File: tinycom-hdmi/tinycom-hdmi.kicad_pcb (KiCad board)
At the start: 2 copper layers, 45.2 x 45.2 mm, 70 parts, among them J1 MICRO_SD_HINGE, P1 CONN_02X10, P2 CONN_02X10, P4 USB_OTG, U1 SY8008BAAC, U2 AXP209, U3 SY8008BAAC, U4 RTL8188, U5 rainsun-antenna, U6 RCLAMP0524P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

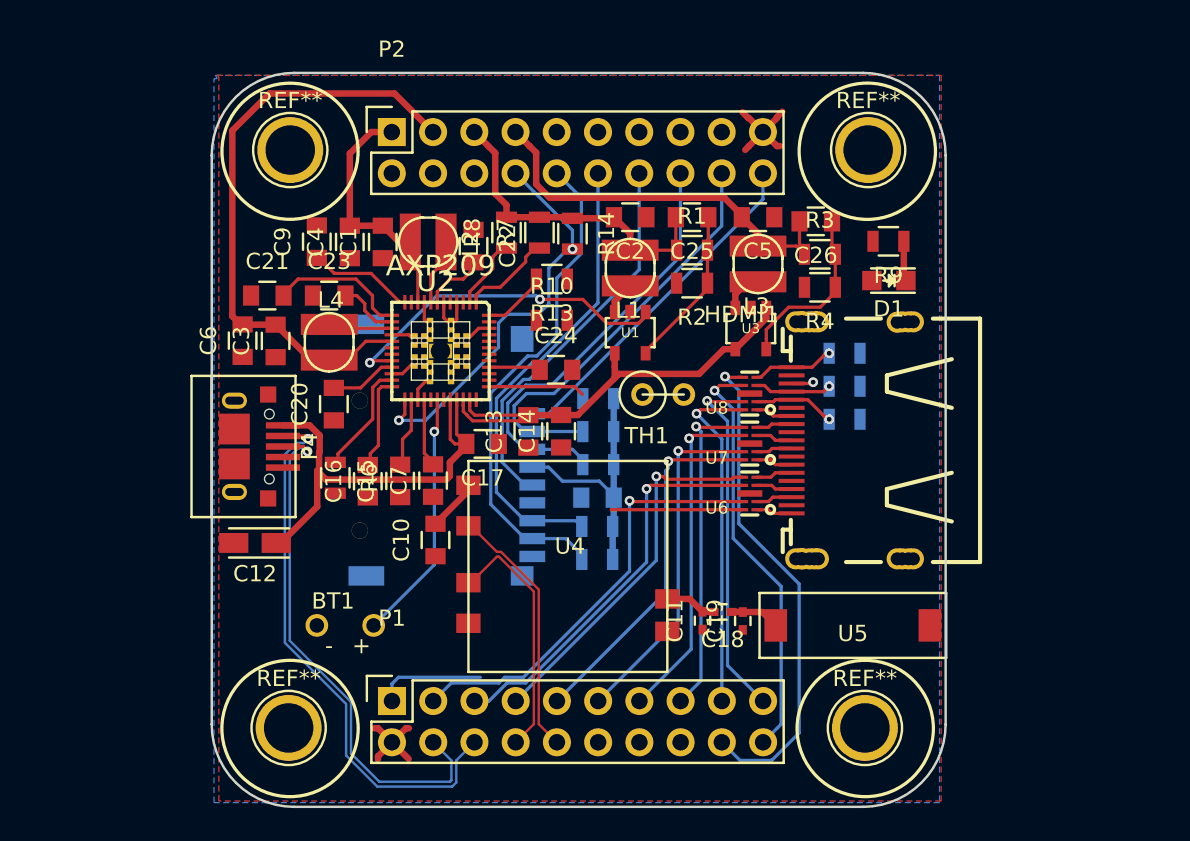
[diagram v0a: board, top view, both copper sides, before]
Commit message: hdmi route
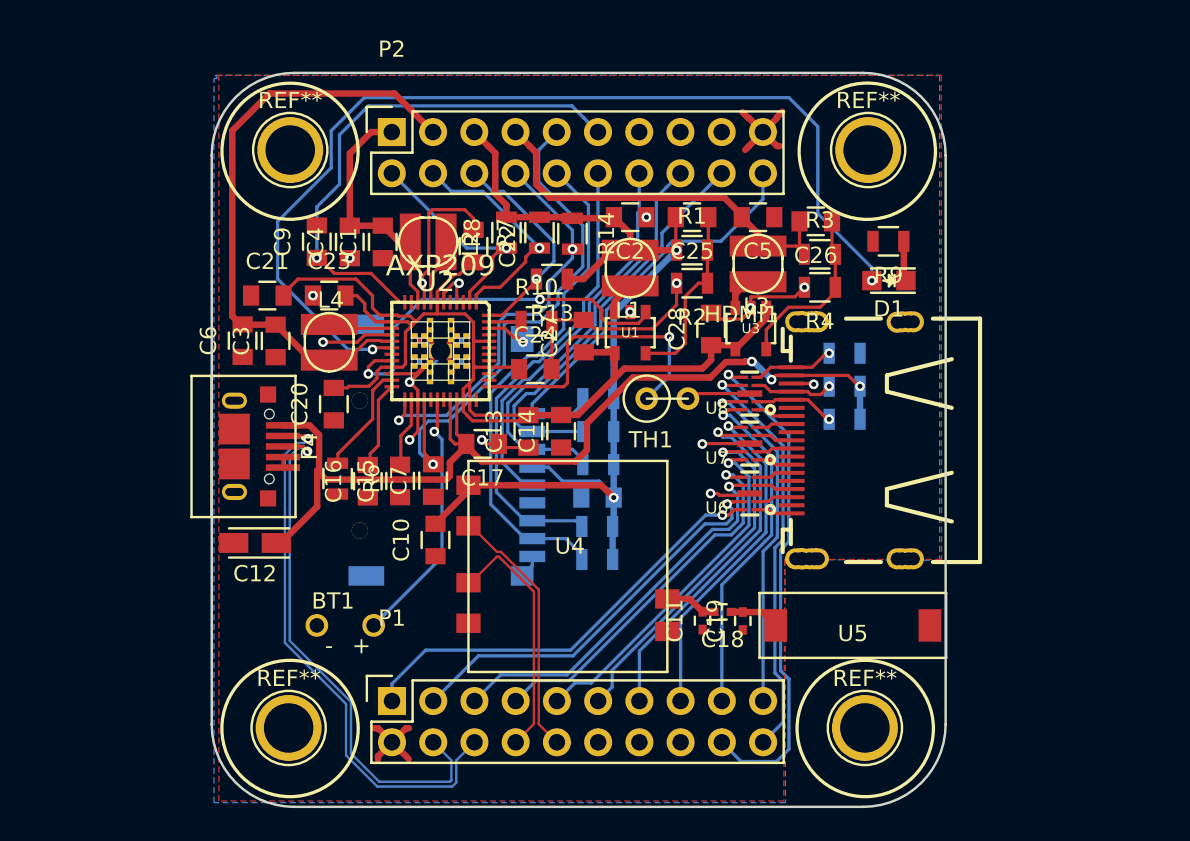
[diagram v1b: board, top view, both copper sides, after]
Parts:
- added C27: 10uF, Capacitors_SMD:C_0805, F.Cu at (147.4, 95.5)
- added C28: 10uF, Capacitors_SMD:C_0805, F.Cu at (155.2, 95.0)
- moved G*** 3.23 mm to (158.1, 93.0)
- moved C24 1.27 mm to (144.4, 97.5)
- moved R10 0.95 mm to (144.5, 94.6)
- moved TH1 0.36 mm to (152.5, 99.3)
- moved R6 0.15 mm to (132.2, 104.2)
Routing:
- net GND: track 24.9 -> 96.9 mm, vias 1 -> 17
- net Net-(D1-Pad2): track 0.00 -> 61.8 mm, vias 0 -> 2
- net +5V: track 27.8 -> 58.8 mm, vias 0 -> 3
- net VCC_13_RTC: track 4.27 -> 32.8 mm, vias 0 -> 1
- net VCC_30_ANL: track 6.55 -> 32.0 mm, vias 0 -> 1
- net VCC_33: track 39.1 -> 63.7 mm, vias 0 -> 2
- net IPSOUT: track 52.7 -> 74.0 mm
- net Net-(TH1-Pad1): track 5.94 -> 18.4 mm, vias 0 -> 1
- net HTX2_P: track 14.8 -> 27.1 mm, vias 0 -> 1
- net NMI_N: track 4.01 -> 13.3 mm, vias 0 -> 1
- net TWI0_SCK: track 4.46 -> 13.4 mm, vias 0 -> 1
- net TWI0_SDA: track 5.72 -> 14.2 mm, vias 0 -> 1
- net SDC0_D2: track 21.3 -> 26.1 mm
- net EXTEN: track 21.2 -> 23.8 mm
- net Net-(R10-Pad1): track 0.00 -> 1.97 mm
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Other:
- net class Default: clearance 0.15 -> 0.14
- net class Power: trace_width 0.4 -> 0.2
- rule trace_clearance: 0.15 -> 0.14

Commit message: improve hdmi
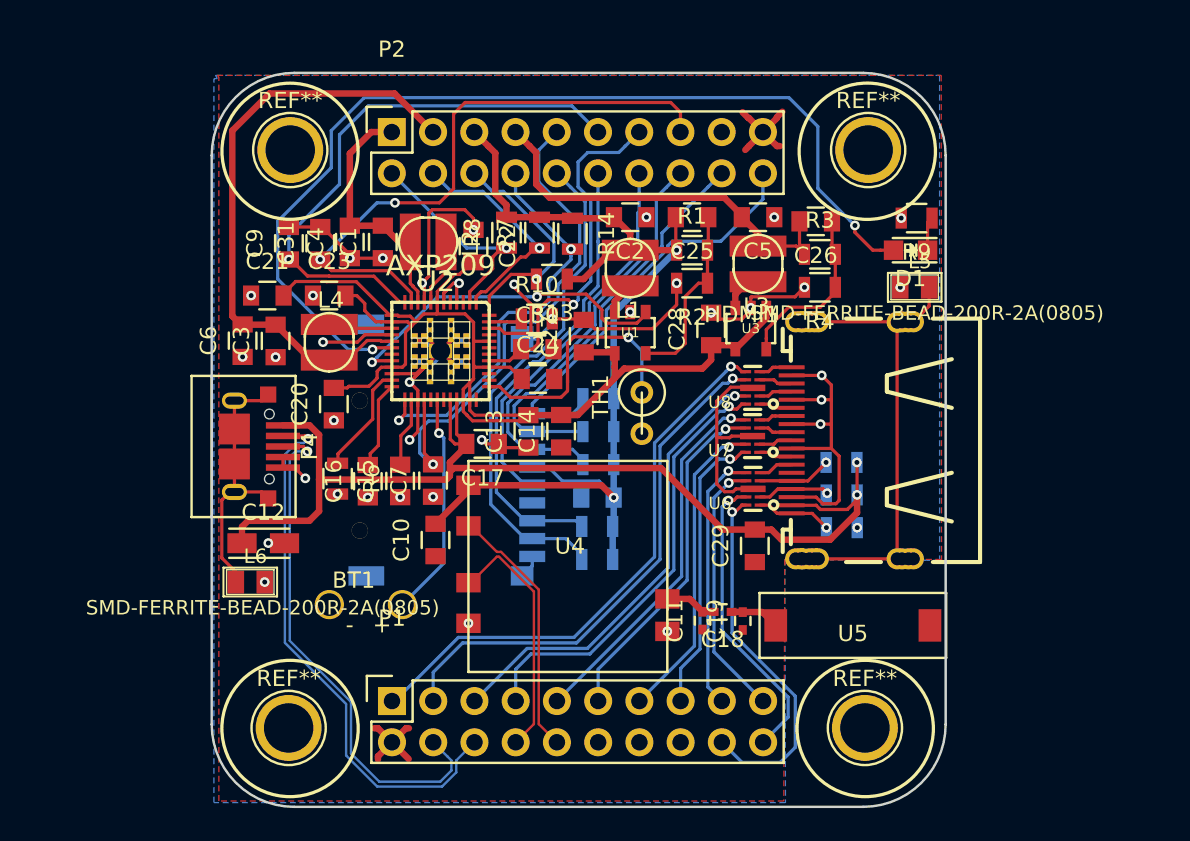
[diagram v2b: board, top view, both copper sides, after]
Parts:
- added C29: 10uF, Capacitors_SMD:C_0805, F.Cu at (157.9, 108.4)
- added C30: C_Small, Capacitors_SMD:C_0805, F.Cu at (144.5, 96.3)
- added C31: C_Small, Capacitors_SMD:C_0805, F.Cu at (131.1, 89.7)
- added L5: SMD-FERRITE-BEAD-200R-2A(0805), OPL-Inductor-L0805, F.Cu at (167.8, 92.5)
- added L6: SMD-FERRITE-BEAD-200R-2A(0805), OPL-Inductor-L0805, F.Cu at (126.8, 110.6)
- R10: value 200K -> 2K
- moved R12 10.7 mm to (163.3, 107.3)
- moved R11 4.69 mm to (163.3, 103.2)
- moved R5 4.66 mm to (163.3, 105.2)
- moved D1 2.30 mm to (167.5, 90.2)
- moved R9 2.25 mm to (167.9, 88.2)
- moved BT1 1.80 mm to (134.0, 112.0)
- moved TH1 1.80 mm to (151.0, 100.2), turned to 270 degrees
- moved C9 1.72 mm to (129.2, 89.7)
- moved C24 0.62 mm to (144.6, 98.1)
- moved C12 0.51 mm to (127.6, 108.2), turned to 0 degrees
- moved U7 0.49 mm to (157.8, 101.6)
- moved U8 0.39 mm to (157.8, 98.7)
- moved U6 0.35 mm to (157.8, 104.9)
- moved R10 0.15 mm to (144.5, 94.4)
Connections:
- net UART1_TX renamed Net-(P2-Pad17)
- HDMI1 pad 11: Net-(HDMI1-Pad11) -> GND
- HDMI1 pad 12: GND -> Net-(HDMI1-Pad12)
- HDMI1 pad 15: GND -> Net-(HDMI1-Pad15)
- HDMI1 pad 17: Net-(HDMI1-Pad17) -> GND
- HDMI1 pad 18: GND -> +5V
- HDMI1 pad 2: +5V -> GND
- HDMI1 pad 3: GND -> Net-(HDMI1-Pad3)
- HDMI1 pad 5: Net-(HDMI1-Pad5) -> GND
- HDMI1 pad 8: Net-(HDMI1-Pad8) -> GND
- HDMI1 pad 9: GND -> Net-(HDMI1-Pad9)
- HDMI1 pad SH2: Net-(HDMI1-PadSH2) -> Net-(HDMI1-PadSH1)
- HDMI1 pad SH3: Net-(HDMI1-PadSH3) -> Net-(HDMI1-PadSH1)
- HDMI1 pad SH4: Net-(HDMI1-PadSH4) -> Net-(HDMI1-PadSH1)
- P2 pad 13: Net-(P2-Pad13) -> LDO3_28
- P2 pad 15: UART1_RX -> LDO4_28
- P4 pad 6: GND -> Net-(L6-Pad1)
- R11 pad 1: Net-(HDMI1-Pad4) -> Net-(HDMI1-Pad15)
- R12 pad 2: Net-(HDMI1-Pad1) -> Net-(HDMI1-Pad19)
- R5 pad 2: Net-(HDMI1-Pad5) -> Net-(HDMI1-Pad16)
- U2 pad 11: Net-(U2-Pad11) -> LDO4_28
- U2 pad 41: Net-(U2-Pad41) -> LDO3_28
- U6 pad 10: HTX2_P -> HHPD
- U6 pad 2: Net-(HDMI1-Pad17) -> Net-(HDMI1-Pad16)
- U6 pad 4: Net-(HDMI1-Pad16) -> Net-(HDMI1-Pad15)
- U6 pad 5: Net-(HDMI1-Pad14) -> Net-(HDMI1-Pad13)
- U6 pad 6: HTX1_N -> HCEC
- U6 pad 7: HTX1_P -> HCSL
- U6 pad 9: HTX2_N -> HSDA
- U7 pad 1: Net-(HDMI1-Pad13) -> Net-(HDMI1-Pad12)
- U7 pad 10: HTX0_P -> HTXC_N
- U7 pad 2: Net-(HDMI1-Pad11) -> Net-(HDMI1-Pad10)
- U7 pad 4: Net-(HDMI1-Pad10) -> Net-(HDMI1-Pad9)
- U7 pad 5: Net-(HDMI1-Pad8) -> Net-(HDMI1-Pad7)
- U7 pad 6: HTXC_N -> HTX0_P
- U7 pad 7: HTXC_P -> HTX0_N
- U7 pad 9: HTX0_N -> HTXC_P
- U8 pad 1: Net-(HDMI1-Pad7) -> Net-(HDMI1-Pad6)
- U8 pad 10: HCEC -> HTX1_N
- U8 pad 2: Net-(HDMI1-Pad5) -> Net-(HDMI1-Pad4)
- U8 pad 4: Net-(HDMI1-Pad4) -> Net-(HDMI1-Pad3)
- U8 pad 6: HHPD -> HTX2_P
- U8 pad 7: HSDA -> HTX2_N
- U8 pad 9: HCSL -> HTX1_P
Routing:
- net LDO4_28: track 0.00 -> 37.1 mm, vias 0 -> 2
- net GND: track 96.9 -> 131.7 mm, vias 17 -> 38
- net Net-(HDMI1-PadSH1): track 0.00 -> 27.1 mm
- net LDO3_28: track 0.00 -> 22.2 mm, vias 0 -> 1
- net Net-(L6-Pad1): track 0.00 -> 16.5 mm
- net HHPD: track 30.9 -> 22.6 mm
- net HTX2_P: track 27.1 -> 34.6 mm
- net +5V: track 58.8 -> 66.1 mm, vias 3 -> 2
- net HSDA: track 25.8 -> 18.5 mm
- net HTX2_N: track 25.8 -> 32.6 mm
- net HCEC: track 21.7 -> 16.2 mm
- net HCSL: track 21.7 -> 16.2 mm
- net Net-(HDMI1-Pad5): track 5.25 -> 0.00 mm, vias 1 -> 0
- net HTX1_P: track 24.0 -> 28.6 mm
- net Net-(HDMI1-Pad15): track 0.00 -> 4.55 mm, vias 0 -> 1
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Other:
- net class Power: trace_width 0.2 -> 0.4
